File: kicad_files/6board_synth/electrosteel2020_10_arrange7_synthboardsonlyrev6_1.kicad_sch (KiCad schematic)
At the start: 81 parts, among them J1 Conn_01x02_Pin, J2 105162-0001, J3 Conn_02x08_Counter_Clockwise, J4 110990030, J5 Conn_02x08_Counter_Clockwise, SW1 B3F-1025, U1 INA2134UA, U2 INA2134UA, U3 INA2134UA, U4 INA2134UA, U5 INA2134UA, U6 OPA1642AIDR, U7 DRV135UA/2K5

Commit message: almost done with circuits, changing sd card reader
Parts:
- removed C15: 22u, Capacitor_SMD:C_Elec_5x5.8, symbol Device:C
- added C17, C18, C20: 4.7uf, electrosteel2020_10_arrange7_synthboardsonlyrev6:C1206K, symbol electrosteel2020_10_arrange7_synthboardsonlyrev6-eagle-import:C-EUC1206K
- added C19: EEE-HP1E220P, Snapeda:CAP_PAN_EEE_D_PAN-L, symbol Snapeda:EEE-HP1E220P
- added J6, J7: 110990030, Connector:NS-Tech_Grove_1x04_P2mm_Vertical, symbol 110990030:110990030
- added J8: MEM2075-00-140-01-A, Snapeda:GCT_MEM2075-00-140-01-A, symbol Snapeda:MEM2075-00-140-01-A
- added L2: 10uH, electrosteel2020_10_arrange7_synthboardsonlyrev6:BOURNS_SRP2010, symbol electrosteel2020_10_arrange7_synthboardsonlyrev6-eagle-import:INDUCTORS
- added R16, R17, R18, R19, R20, R21, R22, R23, R26, R27, R28, R35, R36, R37, R38, R39, R40, R41, R42, R43: 0R, Resistor_SMD:R_0603_1608Metric, symbol Device:R
- added R44: 47R, Resistor_SMD:R_0402_1005Metric, symbol Device:R
- added TP0, TP1, TP2, TP3, TP4, TP5, TP6, TP7, TP8, TP9: TestPoint, Connector_Pin:Pin_D0.9mm_L10.0mm_W2.4mm_FlatFork, symbol Connector:TestPoint
- added U8: RBT05W24S05, Snapeda:RBT10W24S05_XPP_XPR, symbol Snapeda:RBT05W24S05
- C1, C10, C11, C12, C13, C14, C2, C3, C4, C5, C6, C7, C8, C9: value C -> .1uf
- R24, R25: footprint Resistor_SMD:R_0603_1608Metric -> Resistor_SMD:R_0402_1005Metric_Pad0.72x0.64mm_HandSolder
- R29, R3, R30, R31, R32, R33, R34, R93, R94, R95, R96, R97: footprint electrosteel2020_10_arrange7_synthboardsonlyrev6:R0603 -> Resistor_SMD:R_0402_1005Metric_Pad0.72x0.64mm_HandSolder
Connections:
- net +12V: now also C17.1, L2.P$1
- net +3V3: now also J8.P4 (VDD)
- net CLK: now also J8.P5 (CLK)
- net CMD: now also J8.P3 (CMD)
- net DAT0: now also J8.P7 (DAT0)
- net DAT1: now also J8.P8 (DAT1)
- net DAT2: now also J8.P1 (DAT2)
- net DAT3: now also J8.P2 (CD/DAT3)
- net DGND4: now also C20.2, J7.3, J7.4, J8.P6 (VSS), J8.SH1 (SHIELD), J8.SH2 (SHIELD__1), J8.SH3 (SHIELD__2), J8.SH4 (SHIELD__3), U8.2
- net IN_N: now also R17.1, R19.1, R21.1, R23.1, R27.1, R35.1, R37.1, R39.1, R41.1, R43.1; no longer A1.17 (AUDIO_IN_2), A10.17 (AUDIO_IN_2), A2.17 (AUDIO_IN_2), A3.17 (AUDIO_IN_2), A4.17 (AUDIO_IN_2), A5.17 (AUDIO_IN_2), A6.17 (AUDIO_IN_2), A7.17 (AUDIO_IN_2), A8.17 (AUDIO_IN_2), A9.17 (AUDIO_IN_2)
- net IN_P: now also R16.1, R18.1, R20.1, R22.1, R26.1, R28.1, R36.1, R38.1, R40.1, R42.1; no longer A1.16 (AUDIO_IN_1), A10.16 (AUDIO_IN_1), A2.16 (AUDIO_IN_1), A3.16 (AUDIO_IN_1), A4.16 (AUDIO_IN_1), A5.16 (AUDIO_IN_1), A6.16 (AUDIO_IN_1), A7.16 (AUDIO_IN_1), A8.16 (AUDIO_IN_1), A9.16 (AUDIO_IN_1)
- net OUT_PRECAP: now also C19.1
- net PA1_SD_DETECT: now also J8.P9 (CD)
- net at R3.1: now also C19.2
- net SPI6_MISO: now reaches A10.26 (ADC_4)
- net SPI6_MISO: now also R44.1
- net SPI2_NSS: now reaches J5.13 (Pin_13)
- net SPI2_NSS: now also J6.2
- net SPI2_SCK: now reaches J5.14 (Pin_14)
- net SPI2_SCK: now also J6.1
- net SPI2_MISO: now reaches J5.15 (Pin_15)
- net SPI2_MISO: now also J6.3
- net SPI2_MOSI: now reaches J5.16 (Pin_16)
- net SPI2_MOSI: now also J6.4
- net SPI6_MISO_POSTRES: now reaches J5.7 (Pin_7)
- net SPI6_MISO_POSTRES: now also R44.2
- new net: A7.17 (AUDIO_IN_2), R39.2
- new net: A10.16 (AUDIO_IN_1), R16.2, TP0.1
- new net: A5.16 (AUDIO_IN_1), R28.2, TP5.1
- new net: C20.1, J7.1, J7.2, U8.3
- new net: A5.17 (AUDIO_IN_2), R35.2
- new net: A8.16 (AUDIO_IN_1), R40.2, TP8.1
- new net: A10.17 (AUDIO_IN_2), R17.2
- new net: A9.16 (AUDIO_IN_1), R42.2, TP9.1
- new net: A9.17 (AUDIO_IN_2), R43.2
- new net: C18.1, L2.P$2, U8.1
- new net: A3.16 (AUDIO_IN_1), R22.2, TP3.1
- new net: A3.17 (AUDIO_IN_2), R23.2
- new net: A6.17 (AUDIO_IN_2), R37.2
- new net: A1.17 (AUDIO_IN_2), R19.2
- new net: A4.16 (AUDIO_IN_1), R26.2, TP4.1
- new net: A6.16 (AUDIO_IN_1), R36.2, TP6.1
- new net: A1.16 (AUDIO_IN_1), R18.2, TP1.1
- new net: A7.16 (AUDIO_IN_1), R38.2, TP7.1
- new net: A2.16 (AUDIO_IN_1), R20.2, TP2.1
- new net: C17.2, C18.2
- new net: A2.17 (AUDIO_IN_2), R21.2
- new net: A8.17 (AUDIO_IN_2), R41.2
- new net: A4.17 (AUDIO_IN_2), R27.2

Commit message: finished bom and centroid
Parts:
- removed J2: 105162-0001, electrosteel2020_10_arrange7_synthboardsonlyrev6:105162-0001, symbol electrosteel2020_10_arrange7_synthboardsonlyrev6-eagle-import:105162-0001
- L2: footprint electrosteel2020_10_arrange7_synthboardsonlyrev6:BOURNS_SRP2010 -> Inductor_SMD:L_0805_2012Metric

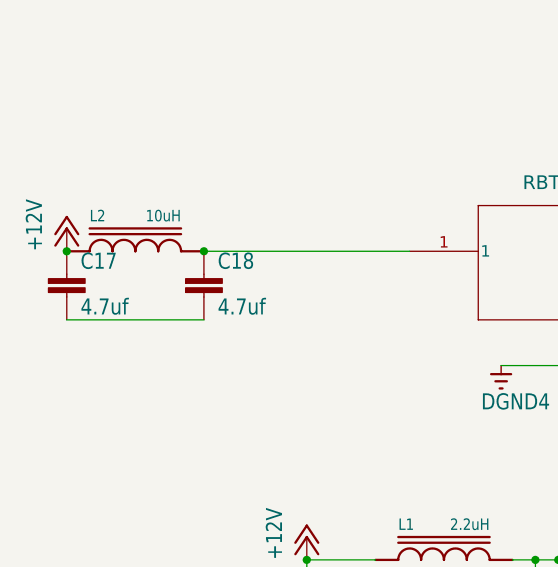
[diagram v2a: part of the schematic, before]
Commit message: got new left hand sensor working with SENT receive on stm32 chip. still requires very wide bar and doesnt yet send to the brain microcontroller or do interpolation
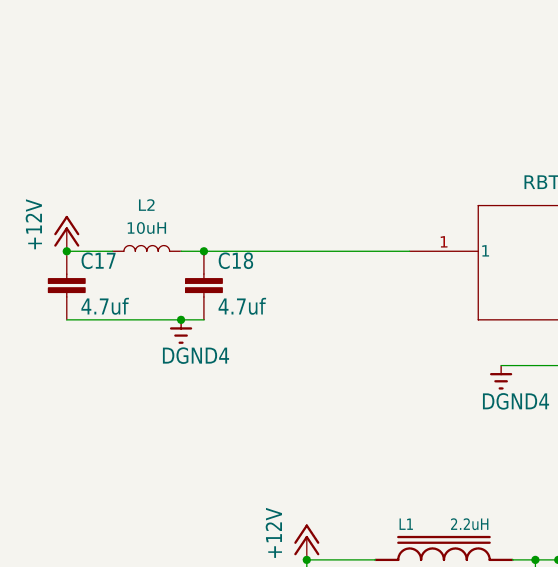
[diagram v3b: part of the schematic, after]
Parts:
- removed L2: 10uH, Inductor_SMD:L_0805_2012Metric, symbol electrosteel2020_10_arrange7_synthboardsonlyrev6-eagle-import:INDUCTORS
- added L2: 10uH, Inductor_SMD:L_0805_2012Metric, symbol Device:L
- R32: footprint Resistor_SMD:R_0402_1005Metric_Pad0.72x0.64mm_HandSolder -> Resistor_SMD:R_0402_1005Metric
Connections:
- net +12V: now also L2.1
- net DGND4: now also C17.2, C18.2
- net at C18.1, U8.1: now also L2.2
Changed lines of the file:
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@@
 	)
 	(junction
+		(at 34.29 204.47)
+		(diameter 0)
+		(color 0 0 0 0)
+	)
+	(junction
 		(at 236.22 20.32)
 		(diameter 0)
@@
 	)
 	(junction
-		(at 34.29 204.47)
+		(at 805.18 52.07)
 		(diameter 0)
 		(color 0 0 0 0)
 	)
 	(junction
-		(at 805.18 52.07)
+		(at 830.58 52.07)
 		(diameter 0)
 		(color 0 0 0 0)
 	)
 	(junction
-		(at 830.58 52.07)
+		(at 403.86 41.91)
 		(diameter 0)
 		(color 0 0 0 0)
 	)
 	(junction
-		(at 403.86 41.91)
+		(at 49.53 204.47)
 		(diameter 0)
 		(color 0 0 0 0)
@@
 	)
 	(junction
+		(at 46.99 212.09)
+		(diameter 0)
+		(color 0 0 0 0)
+	)
+	(junction
 		(at 124.46 243.84)
 		(diameter 0)
@@
 	)
 	(junction
-		(at 49.53 204.47)
-		(diameter 0)
-		(color 0 0 0 0)
-	)
-	(junction
 		(at 124.46 248.92)
 		(diameter 0)
@@
 	(wire
 		(pts
+			(xy 46.99 204.47) (xy 49.53 204.47)
+		)
+		(stroke
+			(width 0)
+			(type default)
+		)
+	)
+	(wire
+		(pts
 			(xy 370.84 184.15) (xy 375.92 184.15)
 		)
@@
 	(wire
 		(pts
+			(xy 34.29 204.47) (xy 39.37 204.47)
+		)
+		(stroke
+			(width 0)
+			(type default)
+		)
+	)
+	(wire
+		(pts
 			(xy 234.95 101.6) (xy 237.49 101.6)
 		)
@@
 	(wire
 		(pts
+			(xy 46.99 212.09) (xy 49.53 212.09)
+		)
+		(stroke
+			(width 0)
+			(type default)
+		)
+	)
+	(wire
+		(pts
 			(xy 843.28 30.48) (xy 855.98 30.48)
 		)
@@
 	(wire
 		(pts
-			(xy 34.29 212.09) (xy 49.53 212.09)
+			(xy 34.29 212.09) (xy 46.99 212.09)
 		)
 		(stroke
@@
 	)
 	(symbol
-		(lib_id "electrosteel2020_10_arrange7_synthboardsonlyrev6-eagle-import:INDUCTORS")
-		(at 41.91 204.47 0)
+		(lib_id "Device:R")
+		(at 675.64 53.34 90)
 		(unit 1)
 		(exclude_from_sim no)
@@
 		(on_board yes)
 		(dnp no)
-		(property "Reference" "L2"
-			(at 36.83 201.295 0)
-			(effects
-				(font
-					(size 1.27 1.0795)
-				)
-				(justify left bottom)
-			)
-		)
-		(property "Value" "10uH"
-			(at 46.99 201.295 0)
+		(fields_autoplaced yes)
+		(property "Reference" "R36"
+			(at 675.64 46.99 90)
 			(effects
 				(font
-					(size 1.27 1.0795)
+					(size 1.27 1.27)
 				)
-				(justify right bottom)
 			)
 		)
-		(property "Footprint" "Inductor_SMD:L_0805_2012Metric"
-			(at 41.91 204.47 0)
+		(property "Value" "0R"
+			(at 675.64 49.53 90)
 			(effects
 				(font
 					(size 1.27 1.27)
 				)
-				(hide yes)
 			)
 		)
-		(property "Datasheet" ""
-			(at 41.91 204.47 0)
+		(property "Footprint" "Resistor_SMD:R_0603_1608Metric"
+			(at 675.64 55.118 90)
 			(effects
 				(font
@@
 			)
 		)
-		(property "Description" ""
-			(at 41.91 204.47 0)
+		(property "Datasheet" "~"
+			(at 675.64 53.34 0)
 			(effects
 				(font
@@
 			)
 		)
-		(property "PARTNO" "SRP2010-2R2M"
-			(at 41.91 204.47 0)
+		(property "Description" "Resistor"
+			(at 675.64 53.34 0)
 			(effects
 				(font
 					(size 1.27 1.27)
 				)
-				(justify left bottom)
 				(hide yes)
 			)
 		)
-		(pin "P$1"
+		(pin "2"
 		)
-		(pin "P$2"
+		(pin "1"
 		)
 		(instances
 			(project "electrosteel2020_10_arrange7_synthboardsonlyrev6"
 				(path "/485604e2-ed4f-49c8-a072-fce68222d950/0b21e4a6-d020-4eb2-8b68-133e5c5b3d86"
-					(reference "L2")
+					(reference "R36")
 					(unit 1)
 				)
@@
 	)
 	(symbol
-		(lib_id "Device:R")
-		(at 675.64 53.34 90)
+		(lib_id "electrosteel2020_10_arrange7_synthboardsonlyrev6-eagle-import:+12V")
+		(at 549.91 36.83 0)
 		(unit 1)
 		(exclude_from_sim no)
@@
 		(on_board yes)
 		(dnp no)
-		(fields_autoplaced yes)
-		(property "Reference" "R36"
-			(at 675.64 46.99 90)
+		(property "Reference" "#P+04"
+			(at 549.91 36.83 0)
 			(effects
 				(font
 					(size 1.27 1.27)
 				)
+				(hide yes)
 			)
 		)
-		(property "Value" "0R"
-			(at 675.64 49.53 90)
+		(property "Value" "+12V"
+			(at 547.37 41.91 90)
 			(effects
 				(font
-					(size 1.27 1.27)
+					(size 1.778 1.5113)
 				)
+				(justify left bottom)
 			)
 		)
-		(property "Footprint" "Resistor_SMD:R_0603_1608Metric"
-			(at 675.64 55.118 90)
+		(property "Footprint" ""
+			(at 549.91 36.83 0)
 			(effects
 				(font
@@
 			)
 		)
-		(property "Datasheet" "~"
-			(at 675.64 53.34 0)
+		(property "Datasheet" ""
+			(at 549.91 36.83 0)
 			(effects
 				(font
@@
 			)
 		)
-		(property "Description" "Resistor"
-			(at 675.64 53.34 0)
+		(property "Description" "SUPPLY SYMBOL"
+			(at 549.91 36.83 0)
 			(effects
 				(font
@@
 			)
 		)
-		(pin "2"
-		)
 		(pin "1"
 		)
@@
 			(project "electrosteel2020_10_arrange7_synthboardsonlyrev6"
 				(path "/485604e2-ed4f-49c8-a072-fce68222d950/0b21e4a6-d020-4eb2-8b68-133e5c5b3d86"
-					(reference "R36")
+					(reference "#P+04")
 					(unit 1)
 				)
@@
 	)
 	(symbol
-		(lib_id "electrosteel2020_10_arrange7_synthboardsonlyrev6-eagle-import:+12V")
-		(at 549.91 36.83 0)
+		(lib_id "Device:L")
+		(at 43.18 204.47 90)
 		(unit 1)
 		(exclude_from_sim no)
@@
 		(on_board yes)
 		(dnp no)
-		(property "Reference" "#P+04"
-			(at 549.91 36.83 0)
+		(fields_autoplaced yes)
+		(property "Reference" "L2"
+			(at 43.18 199.39 90)
 			(effects
 				(font
 					(size 1.27 1.27)
 				)
-				(hide yes)
 			)
 		)
-		(property "Value" "+12V"
-			(at 547.37 41.91 90)
+		(property "Value" "10uH"
+			(at 43.18 201.93 90)
 			(effects
 				(font
-					(size 1.778 1.5113)
+					(size 1.27 1.27)
 				)
-				(justify left bottom)
 			)
 		)
-		(property "Footprint" ""
-			(at 549.91 36.83 0)
+		(property "Footprint" "Inductor_SMD:L_0805_2012Metric"
+			(at 43.18 204.47 0)
 			(effects
 				(font
@@
 			)
 		)
-		(property "Datasheet" ""
-			(at 549.91 36.83 0)
+		(property "Datasheet" "~"
+			(at 43.18 204.47 0)
 			(effects
 				(font
@@
 			)
 		)
-		(property "Description" "SUPPLY SYMBOL"
-			(at 549.91 36.83 0)
+		(property "Description" "Inductor"
+			(at 43.18 204.47 0)
 			(effects
 				(font
@@
 			)
 		)
+		(pin "2"
+		)
 		(pin "1"
 		)
 		(instances
-			(project "electrosteel2020_10_arrange7_synthboardsonlyrev6"
+			(project ""
 				(path "/485604e2-ed4f-49c8-a072-fce68222d950/0b21e4a6-d020-4eb2-8b68-133e5c5b3d86"
-					(reference "#P+04")
+					(reference "L2")
 					(unit 1)
 				)
@@
 			)
 		)
-		(property "Footprint" "Resistor_SMD:R_0402_1005Metric_Pad0.72x0.64mm_HandSolder"
+		(property "Footprint" "Resistor_SMD:R_0402_1005Metric"
 			(at 210.82 45.72 0)
 			(effects
@@
 					(unit 1)
 				)
+			)
+		)
+	)
+	(symbol
+		(lib_id "electrosteel2020_10_arrange7_synthboardsonlyrev6-eagle-import:DGND4")
+		(at 46.99 214.63 0)
+		(unit 1)
+		(exclude_from_sim no)
+		(in_bom yes)
+		(on_board yes)
+		(dnp no)
+		(property "Reference" "#V016"
+			(at 46.99 214.63 0)
+			(effects
+				(font
+					(size 1.27 1.27)
+				)
+				(hide yes)
+			)
+		)
+		(property "Value" "DGND4"
+			(at 44.7675 217.17 0)
+			(effects
+				(font
+					(size 1.778 1.5113)
+				)
+				(justify left bottom)
+			)
+		)
+		(property "Footprint" ""
+			(at 46.99 214.63 0)
+			(effects
+				(font
+					(size 1.27 1.27)
+				)
+				(hide yes)
+			)
+		)
+		(property "Datasheet" ""
+			(at 46.99 214.63 0)
+			(effects
+				(font
+					(size 1.27 1.27)
+				)
+				(hide yes)
+			)
+		)
+		(property "Description" "SUPPLY SYMBOL"
+			(at 46.99 214.63 0)
+			(effects
+				(font
+					(size 1.27 1.27)
+				)
+				(hide yes)
+			)
+		)
+		(pin "1"
+		)
+		(instances
+			(project "electrosteel2020_10_arrange7_synthboardsonlyrev6"
+				(path "/485604e2-ed4f-49c8-a072-fce68222d950/0b21e4a6-d020-4eb2-8b68-133e5c5b3d86"
+					(reference "#V016")
+					(unit 1)
+				)
